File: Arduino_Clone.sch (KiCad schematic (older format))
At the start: 13 parts, among them U1 24LC1025, U2 24LC1025, U3 DS1337+, U4 ATMEGA328P-AU, Y1 Crystal 32 MHz, Y2 Crystal 60 MHz

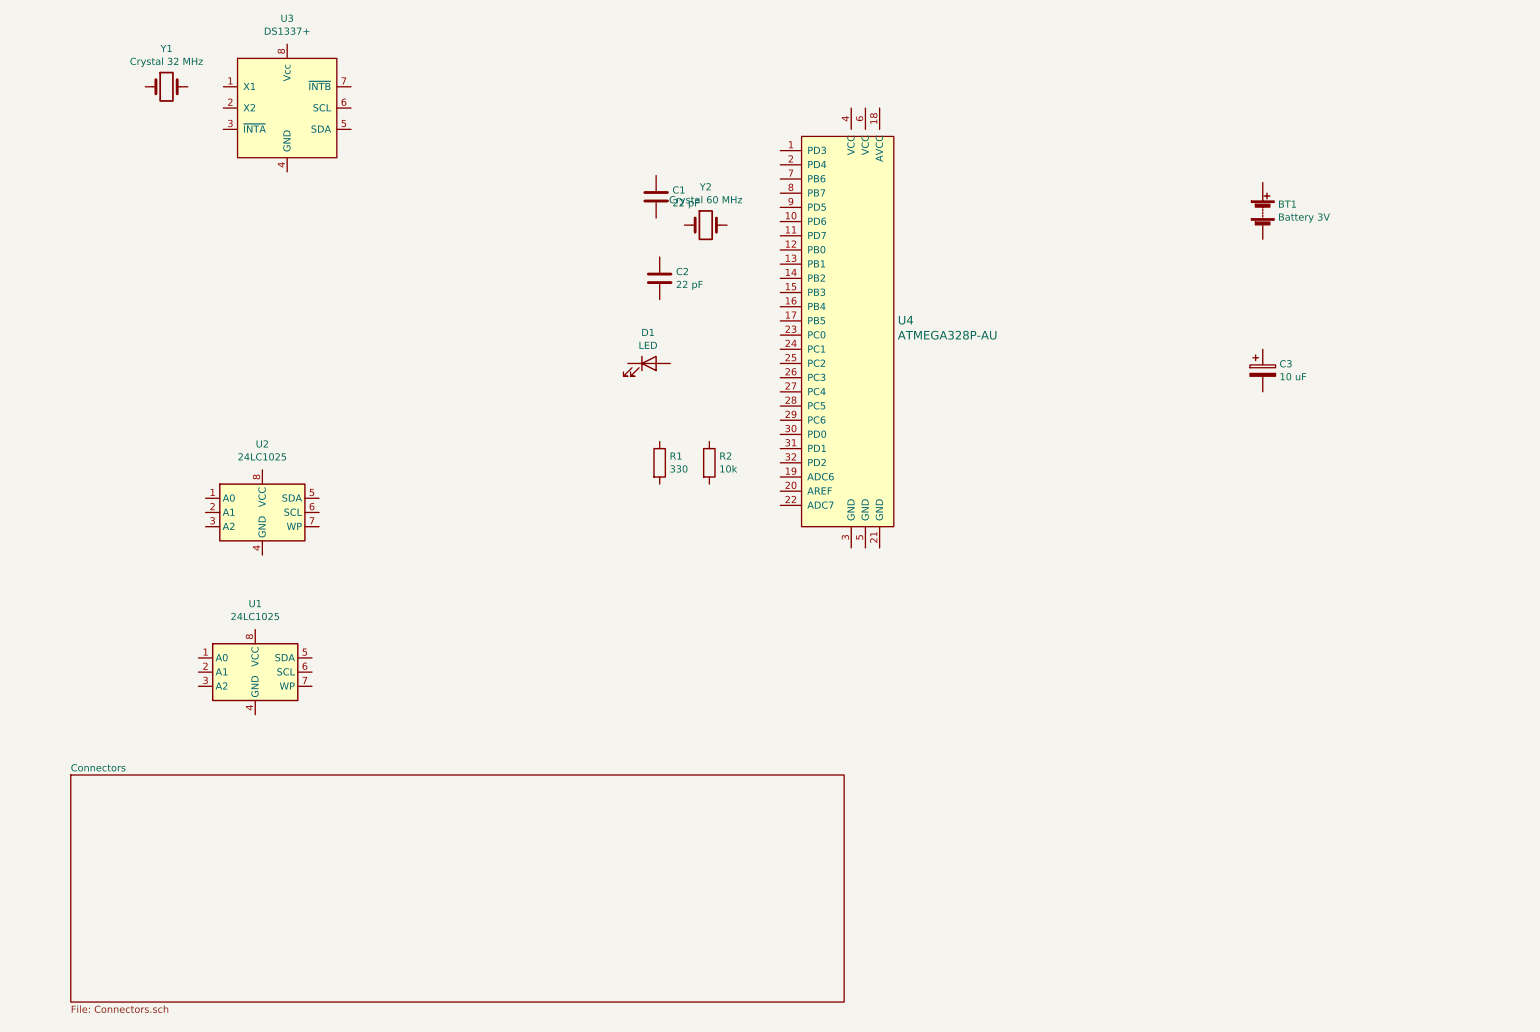
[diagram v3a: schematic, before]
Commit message: Added wiring in connectors sheet.
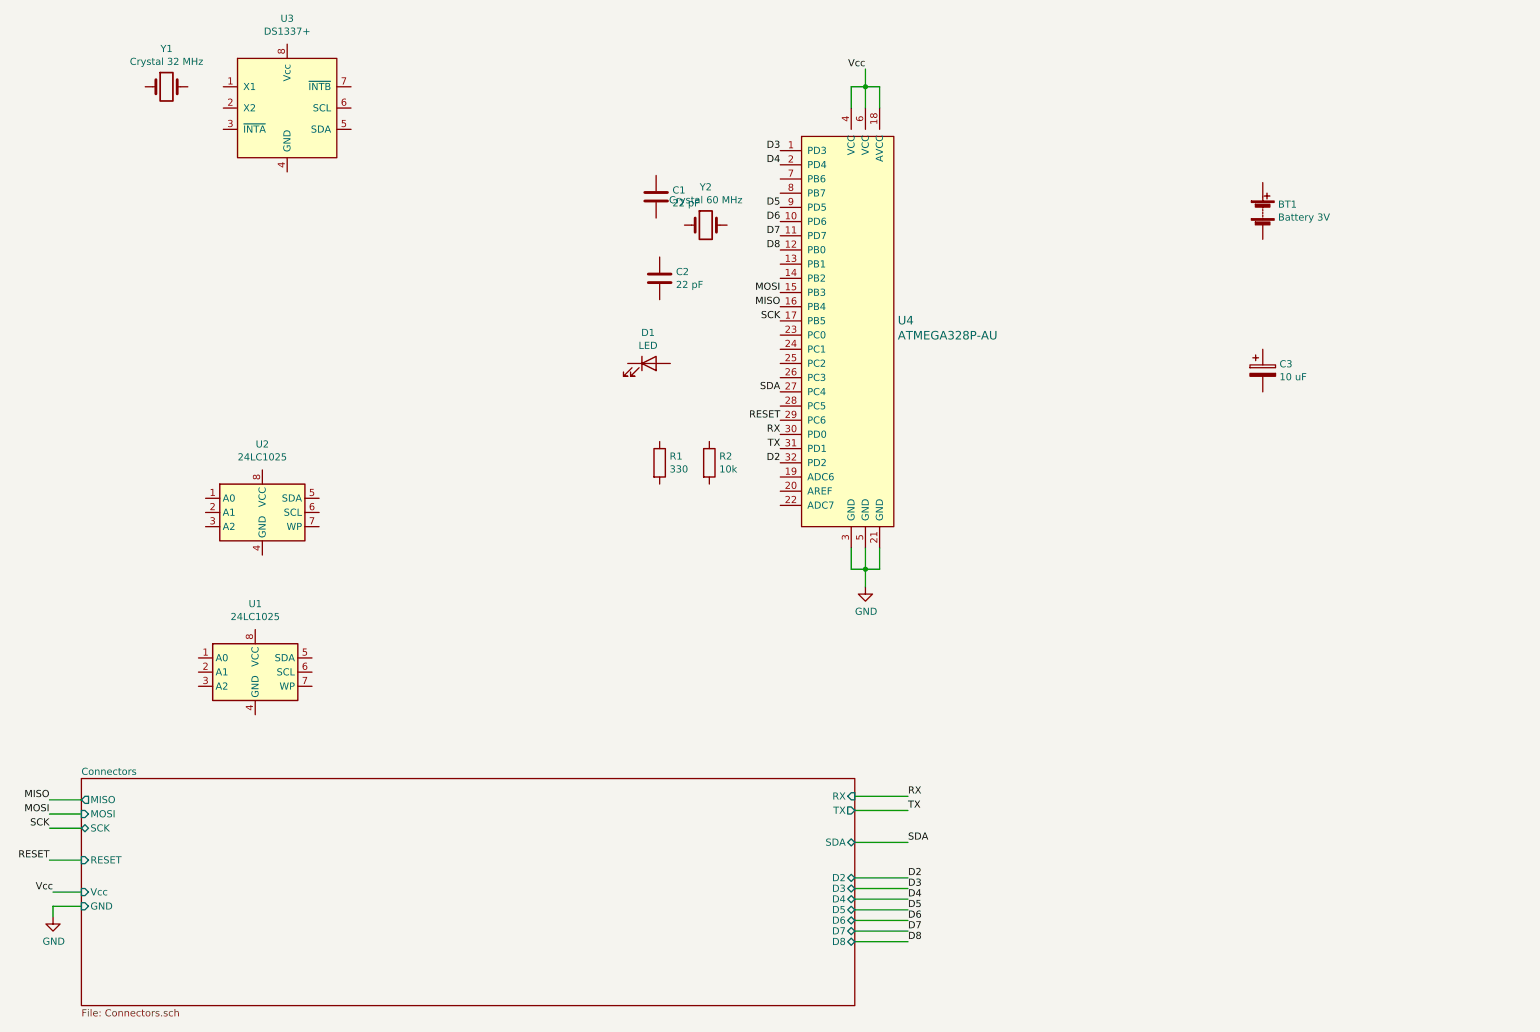
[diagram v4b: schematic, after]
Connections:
- net D3: now reaches U4.1 (PD3)
- net D6: now reaches U4.10 (PD6)
- net D7: now reaches U4.11 (PD7)
- net D8: now reaches U4.12 (PB0)
- net MOSI: now reaches U4.15 (PB3)
- net MISO: now reaches U4.16 (PB4)
- net SCK: now reaches U4.17 (PB5)
- net Vcc: now reaches U4.18 (AVCC)
- net Vcc: now also U4.4 (VCC), U4.6 (VCC)
- net D4: now reaches U4.2 (PD4)
- net GND: now reaches U4.21 (GND)
- net GND: now also U4.3 (GND), U4.5 (GND)
- net SDA: now reaches U4.27 (PC4)
- net RESET: now reaches U4.29 (PC6)
- net RX: now reaches U4.30 (PD0)
- net TX: now reaches U4.31 (PD1)
- net D2: now reaches U4.32 (PD2)
- net D5: now reaches U4.9 (PD5)
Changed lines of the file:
@@
 	1    0    0    -1
 $EndComp
-$Sheet
-S 875  6025 5450 1600
-U 6017416D
-F0 "Connectors" 50
-F1 "Connectors.sch" 50
-$EndSheet
 $Comp
 L My_Library:DS1337_v2 U3
@@
 	1    0    0    -1
 $EndComp
+Text Label 725  6200 2    50   ~ 0
+MISO
+Wire Wire Line
+	725  6200 950  6200
+$Sheet
+S 950  6050 5450 1600
+U 6017416D
+F0 "Connectors" 50
+F1 "Connectors.sch" 50
+F2 "MISO" O L 950 6200 50
+F3 "SCK" B L 950 6400 50
+F4 "RESET" I L 950 6625 50
+F5 "Vcc" I L 950 6850 50
+F6 "MOSI" I L 950 6300 50
+F7 "GND" I L 950 6950 50
+F8 "RX" I R 6400 6175 50
+F9 "TX" O R 6400 6275 50
+F10 "SDA" B R 6400 6500 50
+F11 "D2" B R 6400 6750 50
+F12 "D3" B R 6400 6825 50
+F13 "D5" B R 6400 6975 50
+F14 "D6" B R 6400 7050 50
+F15 "D8" B R 6400 7200 50
+F16 "D4" B R 6400 6900 50
+F17 "D7" B R 6400 7125 50
+$EndSheet
+Text Label 5875 2725 2    50   ~ 0
+MISO
+Text Label 725  6300 2    50   ~ 0
+MOSI
+Text Label 725  6400 2    50   ~ 0
+SCK
+Text Label 725  6625 2    50   ~ 0
+RESET
+Text Label 750  6850 2    50   ~ 0
+Vcc
+Wire Wire Line
+	725  6300 950  6300
+Wire Wire Line
+	725  6400 950  6400
+Wire Wire Line
+	725  6625 950  6625
+Wire Wire Line
+	750  6850 950  6850
+Wire Wire Line
+	750  6950 950  6950
+Text Label 5875 2625 2    50   ~ 0
+MOSI
+Text Label 5875 2825 2    50   ~ 0
+SCK
+Text Label 5875 3525 2    50   ~ 0
+RESET
+Wire Wire Line
+	6375 4425 6375 4575
+Wire Wire Line
+	6575 4575 6575 4425
+Wire Wire Line
+	6375 4575 6475 4575
+Wire Wire Line
+	6475 4425 6475 4575
+Connection ~ 6475 4575
+Wire Wire Line
+	6475 4575 6575 4575
+Wire Wire Line
+	6475 4575 6475 4700
+Wire Wire Line
+	6375 1325 6375 1175
+Wire Wire Line
+	6375 1175 6475 1175
+Wire Wire Line
+	6575 1175 6575 1325
+Wire Wire Line
+	6475 1325 6475 1175
+Connection ~ 6475 1175
+Wire Wire Line
+	6475 1175 6575 1175
+Wire Wire Line
+	6475 1175 6475 1050
+Text Label 6475 1050 2    50   ~ 0
+Vcc
+$Comp
+L power:GND #PWR?
+U 1 1 601A5F49
+P 6475 4700
+F 0 "#PWR?" H 6475 4450 50  0001 C CNN
+F 1 "GND" H 6480 4527 50  0000 C CNN
+F 2 "" H 6475 4700 50  0001 C CNN
+F 3 "" H 6475 4700 50  0001 C CNN
+	1    6475 4700
+	1    0    0    -1
+$EndComp
+Wire Wire Line
+	750  6950 750  7025
+$Comp
+L power:GND #PWR?
+U 1 1 601A6D6C
+P 750 7025
+F 0 "#PWR?" H 750 6775 50  0001 C CNN
+F 1 "GND" H 755 6852 50  0000 C CNN
+F 2 "" H 750 7025 50  0001 C CNN
+F 3 "" H 750 7025 50  0001 C CNN
+	1    750  7025
+	1    0    0    -1
+$EndComp
+Text Label 6775 6175 0    50   ~ 0
+RX
+Text Label 6775 6275 0    50   ~ 0
+TX
+Text Label 6775 6500 0    50   ~ 0
+SDA
+Text Label 6775 6750 0    50   ~ 0
+D2
+Text Label 6775 6900 0    50   ~ 0
+D4
+Text Label 6775 6975 0    50   ~ 0
+D5
+Text Label 6775 7050 0    50   ~ 0
+D6
+Text Label 6775 7125 0    50   ~ 0
+D7
+Text Label 6775 7200 0    50   ~ 0
+D8
+Text Label 6775 6825 0    50   ~ 0
+D3
+Wire Wire Line
+	6400 6175 6775 6175
+Wire Wire Line
+	6400 6275 6775 6275
+Wire Wire Line
+	6400 6500 6775 6500
+Wire Wire Line
+	6775 6750 6400 6750
+Wire Wire Line
+	6400 6825 6775 6825
+Wire Wire Line
+	6775 6900 6400 6900
+Wire Wire Line
+	6775 6975 6400 6975
+Wire Wire Line
+	6775 7050 6400 7050
+Wire Wire Line
+	6400 7125 6775 7125
+Wire Wire Line
+	6775 7200 6400 7200
+Text Label 5875 1625 2    50   ~ 0
+D3
+Text Label 5875 1725 2    50   ~ 0
+D4
+Text Label 5875 2025 2    50   ~ 0
+D5
+Text Label 5875 2125 2    50   ~ 0
+D6
+Text Label 5875 2225 2    50   ~ 0
+D7
+Text Label 5875 2325 2    50   ~ 0
+D8
+Text Label 5875 3325 2    50   ~ 0
+SDA
+Text Label 5875 3625 2    50   ~ 0
+RX
+Text Label 5875 3725 2    50   ~ 0
+TX
+Text Label 5875 3825 2    50   ~ 0
+D2
 $EndSCHEMATC

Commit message: Added more necessary components. Corrected winrings. Generated netlist.
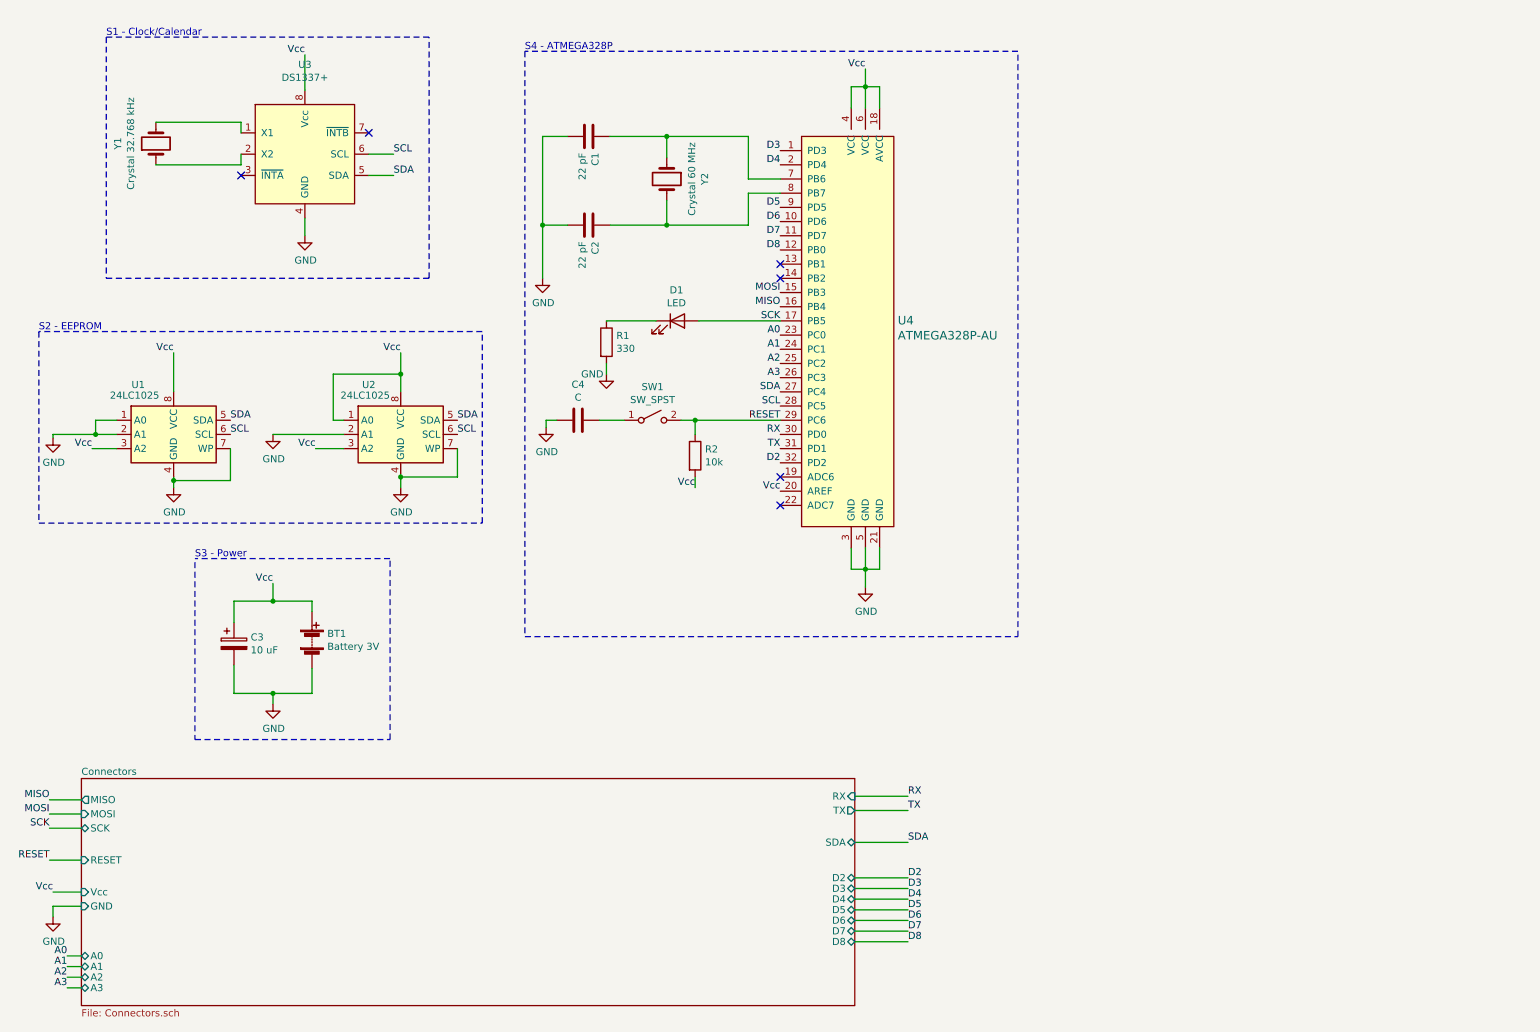
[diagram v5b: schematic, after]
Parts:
- added C4: C, Capacitor_SMD:C_0805_2012Metric_Pad1.18x1.45mm_HandSolder, symbol Device:C
- added SW1: SW_SPST, Button_Switch_SMD:SW_DIP_SPSTx01_Slide_6.7x4.1mm_W6.73mm_P2.54mm_LowProfile_JPin, symbol Switch:SW_SPST
- Y1: value Crystal 32 MHz -> Crystal 32.768 kHz
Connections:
- net GND: now also BT1.2 (-), C1.2, C2.2, C3.2, R1.2, U1.1 (A0), U1.2 (A1), U1.4 (GND), U1.7 (WP), U2.2 (A1), U2.4 (GND), U2.7 (WP), U3.4 (GND), C4.2
- net RESET: now also R2.1, SW1.2 (B)
- net SCK: now also D1.2 (A)
- net SDA: now also U1.5 (SDA), U2.5 (SDA), U3.5 (SDA)
- net Vcc: now also BT1.1 (+), C3.1, R2.2, U1.3 (A2), U1.8 (VCC), U2.1 (A0), U2.3 (A2), U2.8 (VCC), U3.8 (Vcc), U4.20 (AREF)
- net at C1.1: now also U4.7 (PB6), Y2.1
- net at C2.1: now also U4.8 (PB7), Y2.2
- net at D1.1 (K): now also R1.1
- net SCL: now reaches U1.6 (SCL)
- net SCL: now also U2.6 (SCL), U3.6 (SCL), U4.28 (PC5)
- net A0: now reaches U4.23 (PC0)
- net A1: now reaches U4.24 (PC1)
- net A2: now reaches U4.25 (PC2)
- net A3: now reaches U4.26 (PC3)
- net at U3.1 (X1): now also Y1.2
- net at U3.2 (X2): now also Y1.1
- new net: C4.1, SW1.1 (A)
- no-connect marks 0 -> 6
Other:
- note added: "S1 - Clock/Calendar"
- note added: "S2 - EEPROM"
- note added: "S3 - Power"
- note added: "S4 - ATMEGA328P"
- moved on the sheet: BT1, C1, C2, C3, D1, R1, R2, U1, U2, U3, Y1, Y2

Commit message: First version of placements on PCB layout
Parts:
- BT1: footprint Capacitor_SMD:C_0805_2012Metric -> Connector_PinHeader_2.54mm:PinHeader_1x02_P2.54mm_Vertical
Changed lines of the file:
@@
 F 0 "BT1" H 2683 5121 50  0000 L CNN
 F 1 "Battery 3V" H 2683 5030 50  0000 L CNN
-F 2 "Capacitor_SMD:C_0805_2012Metric" V 2575 5135 50  0001 C CNN
+F 2 "Connector_PinHeader_2.54mm:PinHeader_1x02_P2.54mm_Vertical" V 2575 5135 50  0001 C CNN
 F 3 "~" V 2575 5135 50  0001 C CNN
 	1    2575 5075

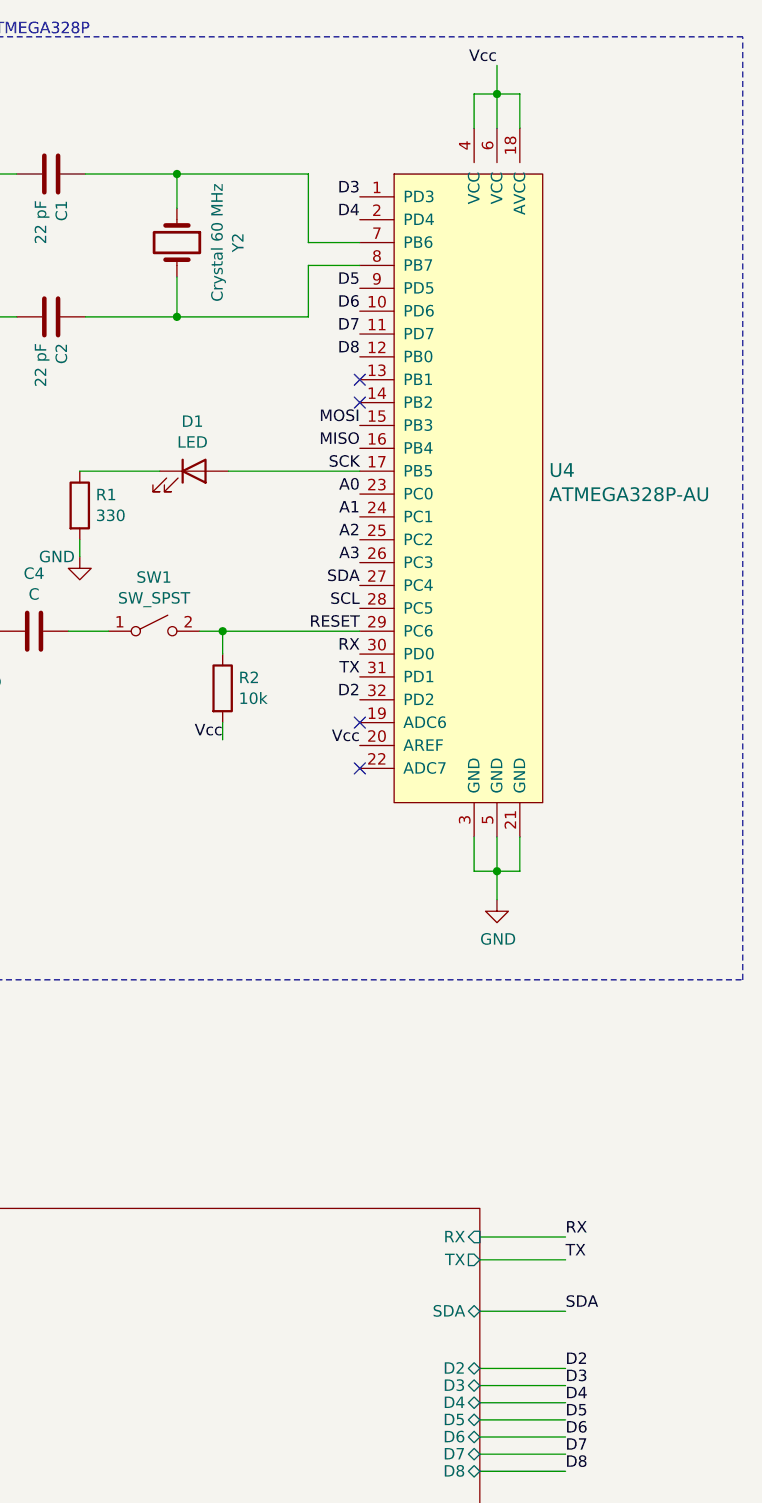
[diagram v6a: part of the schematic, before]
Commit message: Finished PCB Layout.
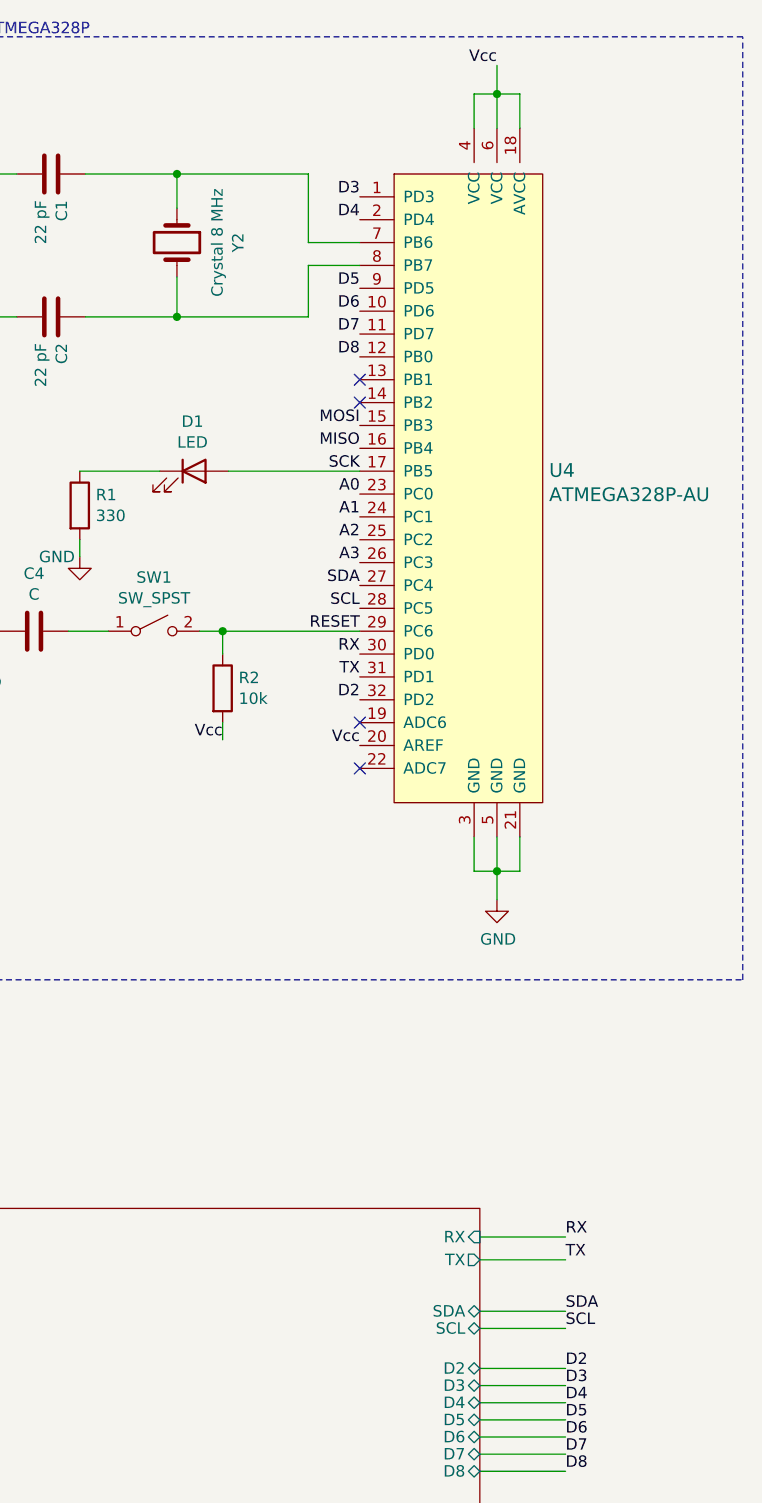
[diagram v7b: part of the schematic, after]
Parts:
- SW1: footprint Button_Switch_SMD:SW_DIP_SPSTx01_Slide_6.7x4.1mm_W6.73mm_P2.54mm_LowProfile_JPin -> Footprints:SPST_SW
- Y2: value Crystal 60 MHz -> Crystal 8 MHz
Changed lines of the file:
@@
 P 5075 1825
 F 0 "Y2" H 5075 2093 50  0000 C CNN
-F 1 "Crystal 60 MHz" H 5075 2002 50  0000 C CNN
+F 1 "Crystal 8 MHz" H 5075 2002 50  0000 C CNN
 F 2 "Crystal:Crystal_SMD_5032-2Pin_5.0x3.2mm_HandSoldering" H 5075 1825 50  0001 C CNN
 F 3 "~" H 5075 1825 50  0001 C CNN
@@
 F20 "A2" B L 950 7450 50
 F21 "A3" B L 950 7525 50
+F22 "SCL" B R 6400 6575 50
 $EndSheet
 Text Label 5875 2725 2    50   ~ 0
@@
 F 0 "SW1" H 4975 3760 50  0000 C CNN
 F 1 "SW_SPST" H 4975 3669 50  0000 C CNN
-F 2 "Button_Switch_SMD:SW_DIP_SPSTx01_Slide_6.7x4.1mm_W6.73mm_P2.54mm_LowProfile_JPin" H 4975 3525 50  0001 C CNN
+F 2 "Footprints:SPST_SW" H 4975 3525 50  0001 C CNN
 F 3 "~" H 4975 3525 50  0001 C CNN
 	1    4975 3525
 	1    0    0    -1
 $EndComp
+Wire Wire Line
+	6400 6575 6775 6575
+Text Label 6775 6575 0    50   ~ 0
+SCL
 $EndSCHEMATC
